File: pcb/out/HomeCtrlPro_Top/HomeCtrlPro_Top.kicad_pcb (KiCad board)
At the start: 2 copper layers, 274 x 141 mm, 77 parts, among them J1 B2B, J10 RS485, J11 CAN, J12 TFT, J2 Wejscia 0-3, J3 Wejscia 4-7, J4 Wejscia 8-11, J5 Wejscia 12-15, J6 Wejscia 16-19, J7 Wejscia 20-23, J8 Wejscia 24-27, J9 Wejscia 28-31, SW1 RST, SW2 BOOT, U1 ESP32-C3-MINI-1, U2 MCP23017, U3 MCP23017, U4 MAX485, U5 TJA1051

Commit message: ESP32-S3 + przyciski TFT; kompaktowy layout (szerokosc z liczby zlacz, 2 rzedy)
- Przejscie ESP32-C3 -> ESP32-S3 (duzo GPIO): niezalezne RS485/CAN, dotyk z IRQ,
  4 przyciski nawigacji TFT (GORA/DOL/OK/WSTECZ). Nowa czesc ESP32-S3-WROOM-1.
- Layout: I/O wzdluz krawedzi w 2 rzedach (podwojne w pionie), szerokosc plytki
  wynika z LICZBY zlacz (zmienne szerokosci kolumn) - wejscia na gornej krawedzi,
  wyjscia (zaciski) na dolnej. auto_frame() dobiera ciasna wspolna ramke.
- Przekazniki pakowane w strefe 230V (kilka rzedow) omijajaca otwory.
- HomeCtrlPro: 280x185 -> 168x192 mm, mniej pustego miejsca. Oba 0/0/0.

Testy 12/12, zwalidowane kiutils. Bloki: esp32s3, button.

Co-Authored-By: Claude Opus 4.8 (1M context) <noreply@anthropic.com>
Claude-Session: https://claude.ai/code/session_01LNGxtK2Jv1rJLBLPTwFQ9C
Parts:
- added C8: 100nF, pcbforge:C_0805, F.Cu at (144.0, 103.9)
- added R11: 120, pcbforge:R_0805, F.Cu at (123.5, 103.9)
- added R12: 560, pcbforge:R_0805, F.Cu at (127.4, 103.9)
- added R13: 560, pcbforge:R_0805, F.Cu at (131.3, 103.9)
- added R14: 120, pcbforge:R_0805, F.Cu at (147.9, 103.9)
- added SW3: GORA, pcbforge:SW_Push_6mm, F.Cu at (18.0, 42.1)
- added SW4: DOL, pcbforge:SW_Push_6mm, F.Cu at (36.5, 59.1)
- added SW5: OK, pcbforge:SW_Push_6mm, F.Cu at (26.0, 42.1)
- added SW6: WSTECZ, pcbforge:SW_Push_6mm, F.Cu at (44.5, 59.1)
- J2: value Wejscia 0-3 -> We 0-3
- J3: value Wejscia 4-7 -> We 4-7
- J4: value Wejscia 8-11 -> We 8-11
- J5: value Wejscia 12-15 -> We 12-15
- J6: value Wejscia 16-19 -> We 16-19
- J7: value Wejscia 20-23 -> We 20-23
- J8: value Wejscia 24-27 -> We 24-27
- J9: value Wejscia 28-31 -> We 28-31
- R10, R7: value 120 -> 10k
- R8, R9: value 560 -> 10k
- U1: value ESP32-C3-MINI-1 -> ESP32-S3-WROOM-1; footprint pcbforge:ESP32-C3-MINI-1 -> pcbforge:ESP32-S3-WROOM-1
- moved D31 168.4 mm to (111.0, 103.9)
- moved D30 167.9 mm to (106.7, 103.9)
- moved D29 167.5 mm to (102.2, 103.9)
- moved D28 167.0 mm to (97.8, 103.9)
- moved D27 166.5 mm to (93.5, 103.9)
- moved D26 166.0 mm to (89.0, 103.9)
- moved D25 165.6 mm to (84.7, 103.9)
- moved D24 165.1 mm to (80.2, 103.9)
- moved D23 164.6 mm to (75.8, 103.9)
- moved D22 164.2 mm to (71.5, 103.9)
- moved D21 163.7 mm to (67.0, 103.9)
- moved D20 163.2 mm to (62.6, 103.9)
- moved D19 162.8 mm to (58.2, 103.9)
- moved D18 162.3 mm to (53.9, 103.9)
- moved D17 161.8 mm to (49.5, 103.9)
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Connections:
- C3 pad 1: EN -> 3V3
- C4 pad 1: 3V3 -> EN
- J12 pad 11: 3V3 -> TOUCH_IRQ
- J12 pad 4: 3V3 -> TFT_RST
- R10 pad 1: CAN_H -> 3V3
- R10 pad 2: CAN_L -> BTN_BACK
- R2 pad 2: IO9 -> IO0
- R7 pad 1: RS485_A -> 3V3
- R7 pad 2: RS485_B -> BTN_UP
- R8 pad 2: RS485_A -> BTN_DOWN
- R9 pad 1: RS485_B -> 3V3
- R9 pad 2: GND -> BTN_OK
- SW2 pad 1: IO9 -> IO0
- SW2 pad 2: IO9 -> IO0
- U1 pad 10: SPI_MOSI -> BTN_UP
- U1 pad 11: TFT_CS -> BTN_DOWN
- U1 pad 13: IO9 -> SCL
- U1 pad 14: SCL -> TFT_CS
- U1 pad 15: (no net) -> SPI_MOSI
- U1 pad 16: (no net) -> SPI_SCK
- U1 pad 17: RS485_RXD -> SPI_MISO
- U1 pad 18: RS485_TXD -> TFT_DC
- U1 pad 19: GND -> BTN_OK
- U1 pad 4: CAN_TXD -> IO0
- U1 pad 5: RS485_DE -> (no net)
- U1 pad 6: TOUCH_CS -> (no net)
- U1 pad 7: TFT_DC -> (no net)
- U1 pad 8: SPI_SCK -> CAN_TXD
- U1 pad 9: SPI_MISO -> CAN_RXD
- U2 pad 20: (no net) -> EXP_INT
- U3 pad 20: (no net) -> EXP_INT
- U5 pad 4: IO9 -> CAN_RXD
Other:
- board size 274 x 141 mm -> 162 x 116.6 mm

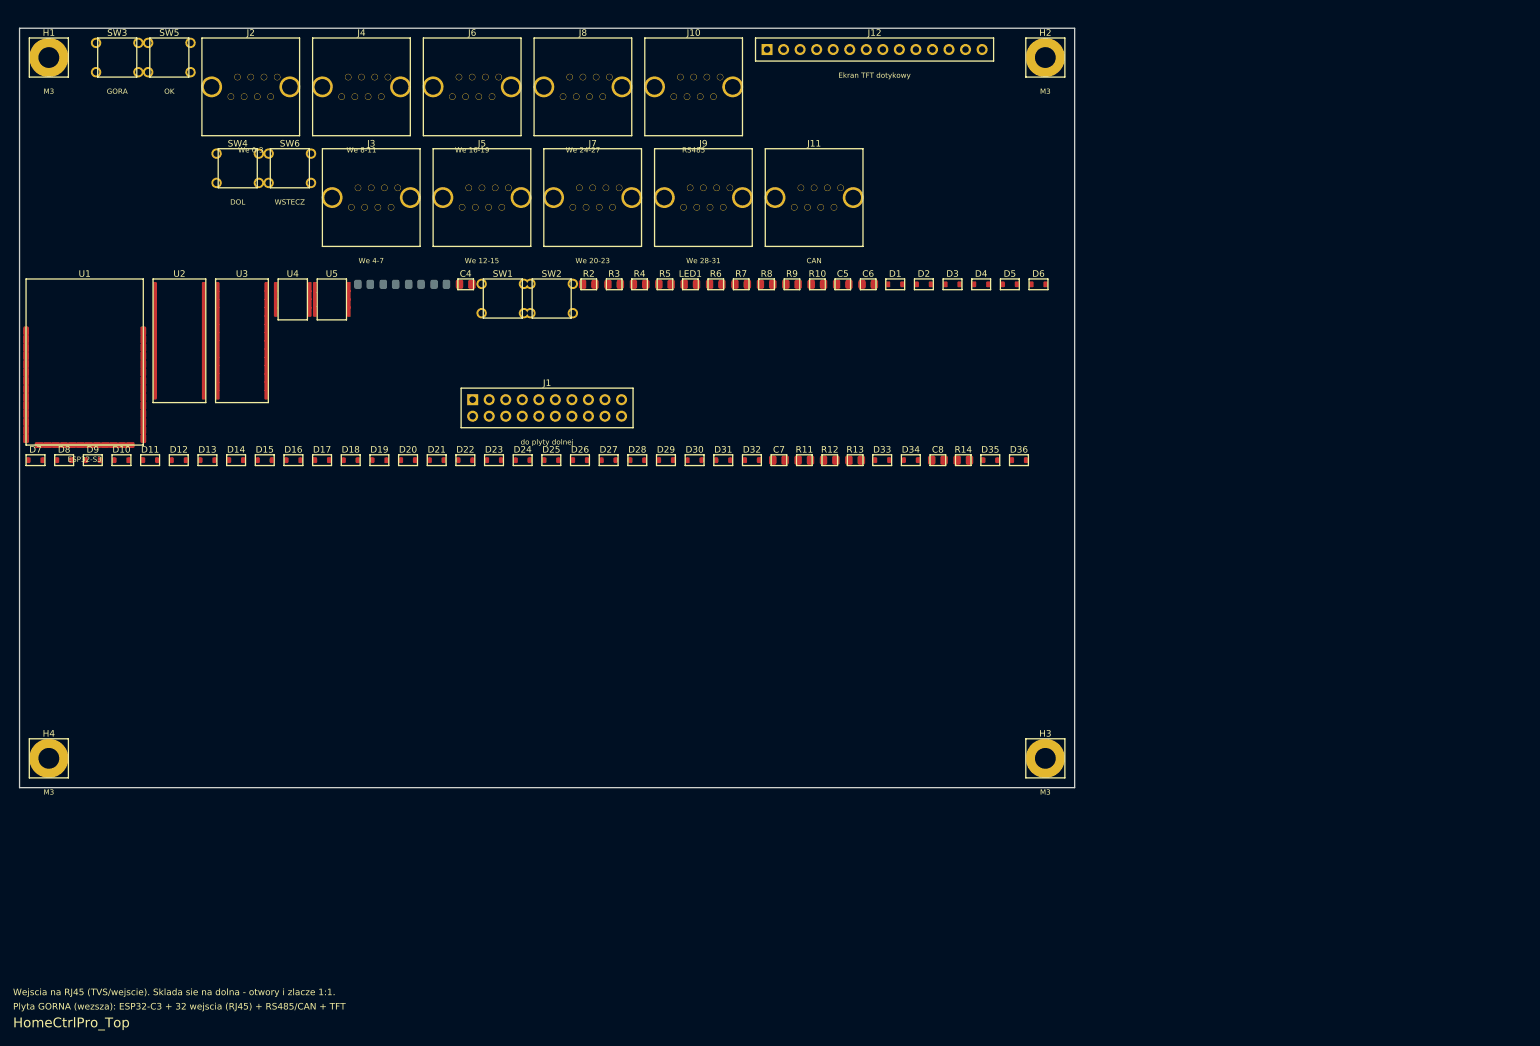
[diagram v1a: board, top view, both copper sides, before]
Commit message: Wejscia w jednym rzedzie PRZY krawedzi + gniazda RJ45 podwojne (2 porty w pionie)
Poprawka po blednej interpretacji: I/O ustawiane w JEDNYM rzedzie zlicowanym do
krawedzi (koniec ze stosowaniem zlacz w 2 rzedach do wnetrza). Szerokosc plytki
= suma szerokosci zlacz w rzedzie. Nowa czesc RJ45_Dual (2 porty RJ45 w jednej
obudowie, jeden nad drugim) + blok input_bank_dual (8 wejsc/gniazdo, TVS/wejscie).
HomeCtrlPro: 4 podwojne RJ45 = 32 wejscia. Oba PCB 0/0/0, testy 12/12, kiutils OK.

Co-Authored-By: Claude Opus 4.8 (1M context) <noreply@anthropic.com>
Claude-Session: https://claude.ai/code/session_01LNGxtK2Jv1rJLBLPTwFQ9C
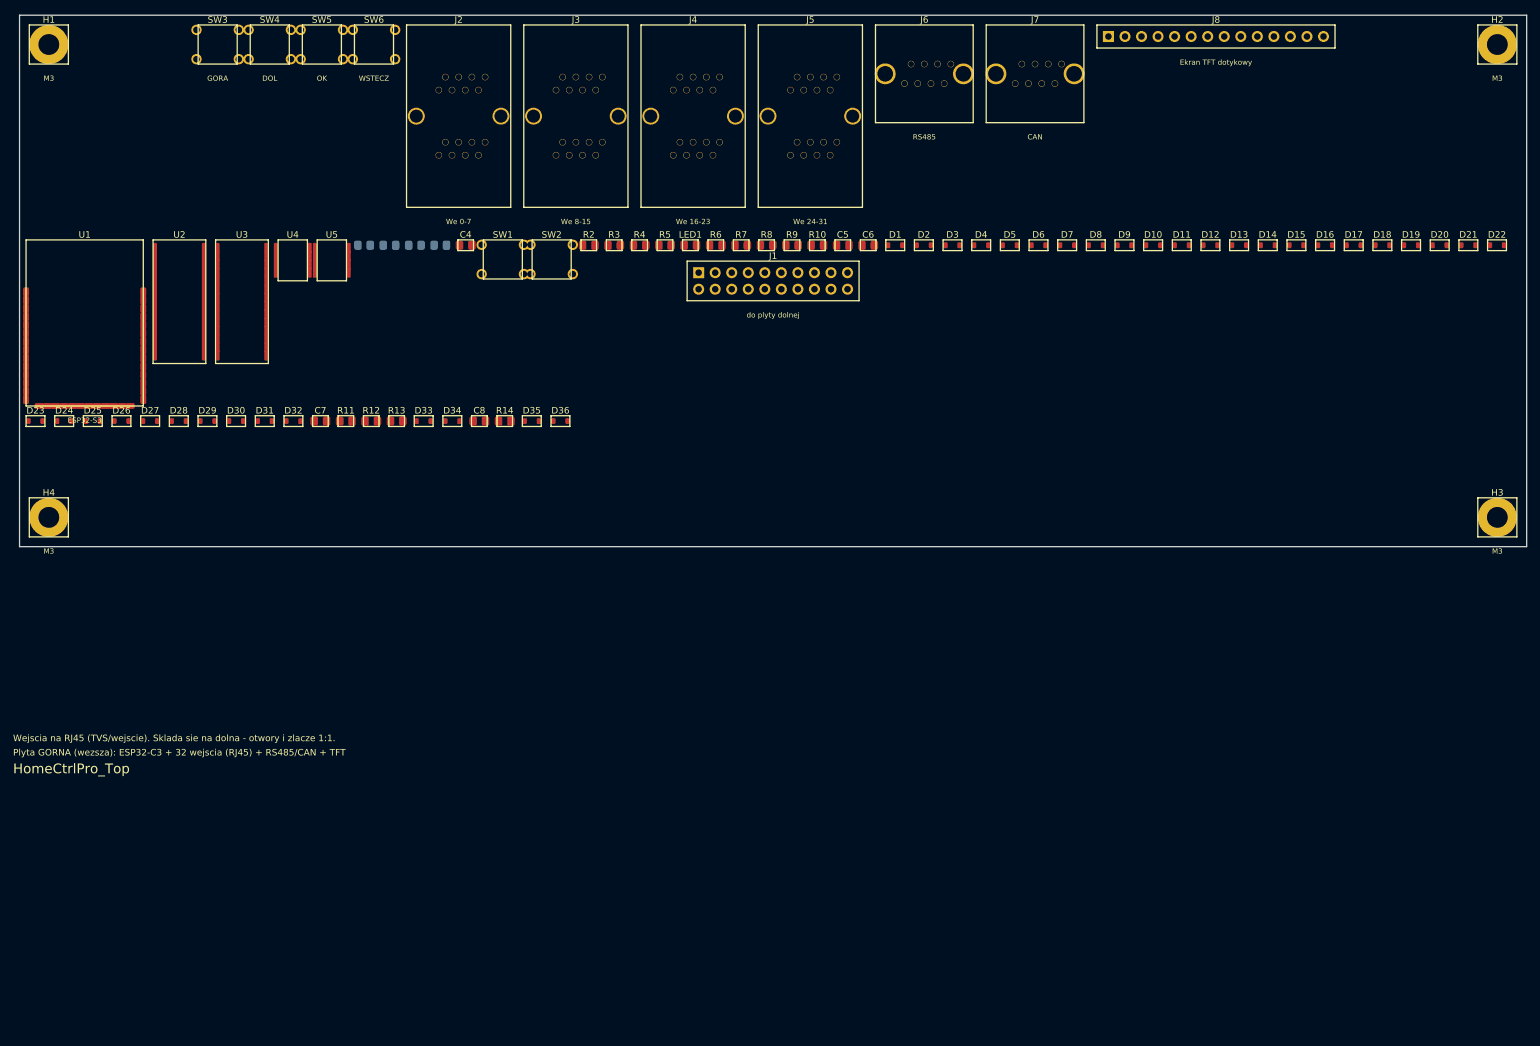
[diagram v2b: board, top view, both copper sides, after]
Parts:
- removed J10: RS485, pcbforge:RJ45_8P8C
- removed J11: CAN, pcbforge:RJ45_8P8C
- removed J12: TFT, pcbforge:PinHeader_1x14_P2.54mm
- removed J9: We 28-31, pcbforge:RJ45_8P8C
- J2: value We 0-3 -> We 0-7; footprint pcbforge:RJ45_8P8C -> pcbforge:RJ45_Dual
- J3: value We 4-7 -> We 8-15; footprint pcbforge:RJ45_8P8C -> pcbforge:RJ45_Dual
- J4: value We 8-11 -> We 16-23; footprint pcbforge:RJ45_8P8C -> pcbforge:RJ45_Dual
- J5: value We 12-15 -> We 24-31; footprint pcbforge:RJ45_8P8C -> pcbforge:RJ45_Dual
- J6: value We 16-19 -> RS485
- J7: value We 20-23 -> CAN
- J8: value We 24-27 -> TFT; footprint pcbforge:RJ45_8P8C -> pcbforge:PinHeader_1x14_P2.54mm
- moved D10 161.8 mm to (177.1, 70.9)
- moved D12 161.8 mm to (185.8, 70.9)
- moved D13 161.8 mm to (190.2, 70.9)
- moved D14 161.8 mm to (194.7, 70.9)
- moved D15 161.8 mm to (199.1, 70.9)
- moved D18 161.8 mm to (212.2, 70.9)
- moved D19 161.8 mm to (216.7, 70.9)
- moved D20 161.8 mm to (221.1, 70.9)
- moved D7 161.8 mm to (163.8, 70.9)
- moved D8 161.8 mm to (168.2, 70.9)
- moved D9 161.8 mm to (172.7, 70.9)
- moved D11 161.8 mm to (181.4, 70.9)
- moved D16 161.8 mm to (203.4, 70.9)
- moved D17 161.8 mm to (207.8, 70.9)
- moved D21 161.8 mm to (225.4, 70.9)
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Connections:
- J3 pad 2: IN4 -> IN8
- J3 pad 3: IN5 -> IN9
- J3 pad 4: IN6 -> IN10
- J3 pad 5: IN7 -> IN11
- J4 pad 2: IN8 -> IN16
- J4 pad 3: IN9 -> IN17
- J4 pad 4: IN10 -> IN18
- J4 pad 5: IN11 -> IN19
- J5 pad 2: IN12 -> IN24
- J5 pad 3: IN13 -> IN25
- J5 pad 4: IN14 -> IN26
- J5 pad 5: IN15 -> IN27
- J6 pad 1: 3V3 -> RS485_A
- J6 pad 2: IN16 -> RS485_B
- J6 pad 3: IN17 -> GND
- J6 pad 4: IN18 -> GND
- J6 pad 5: IN19 -> GND
- J6 pad 7: GND -> 3V3
- J6 pad 8: GND -> 3V3
- J7 pad 1: 3V3 -> CAN_H
- J7 pad 2: IN20 -> CAN_L
- J7 pad 3: IN21 -> GND
- J7 pad 4: IN22 -> GND
- J7 pad 5: IN23 -> GND
- J7 pad 7: GND -> 3V3
- J7 pad 8: GND -> 3V3
- J8 pad 1: 3V3 -> GND
- J8 pad 2: IN24 -> 3V3
- J8 pad 3: IN25 -> TFT_CS
- J8 pad 4: IN26 -> TFT_RST
- J8 pad 5: IN27 -> TFT_DC
- J8 pad 6: GND -> SPI_MOSI
- J8 pad 7: GND -> SPI_SCK
- J8 pad 8: GND -> 3V3
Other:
- board size 162 x 116.6 mm -> 231.4 x 81.6 mm
